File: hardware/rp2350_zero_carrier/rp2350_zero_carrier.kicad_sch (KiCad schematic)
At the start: 8 parts, among them J1 RP2350-Zero_Header(20pin,plac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, J2 USB-A_Host(Neltron_5075AR-04-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, SW1 1回路2接点スイッチ(3pin,NKK_115643,ON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, SW2 1回路2接点スイッチ(3pin,NKK_115643,ON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, SW3 1回路2接点スイッチ(3pin,NKK_115643,ON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

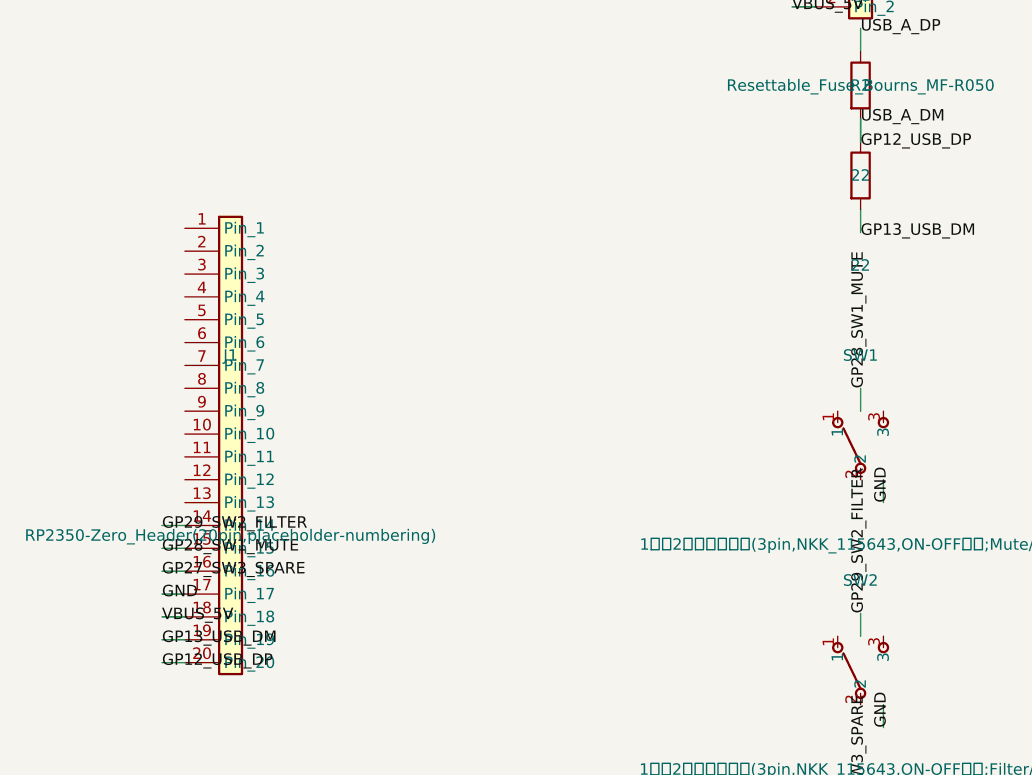
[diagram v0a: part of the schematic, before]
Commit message: feat: unify game mode and add Sumeru lyre mapping
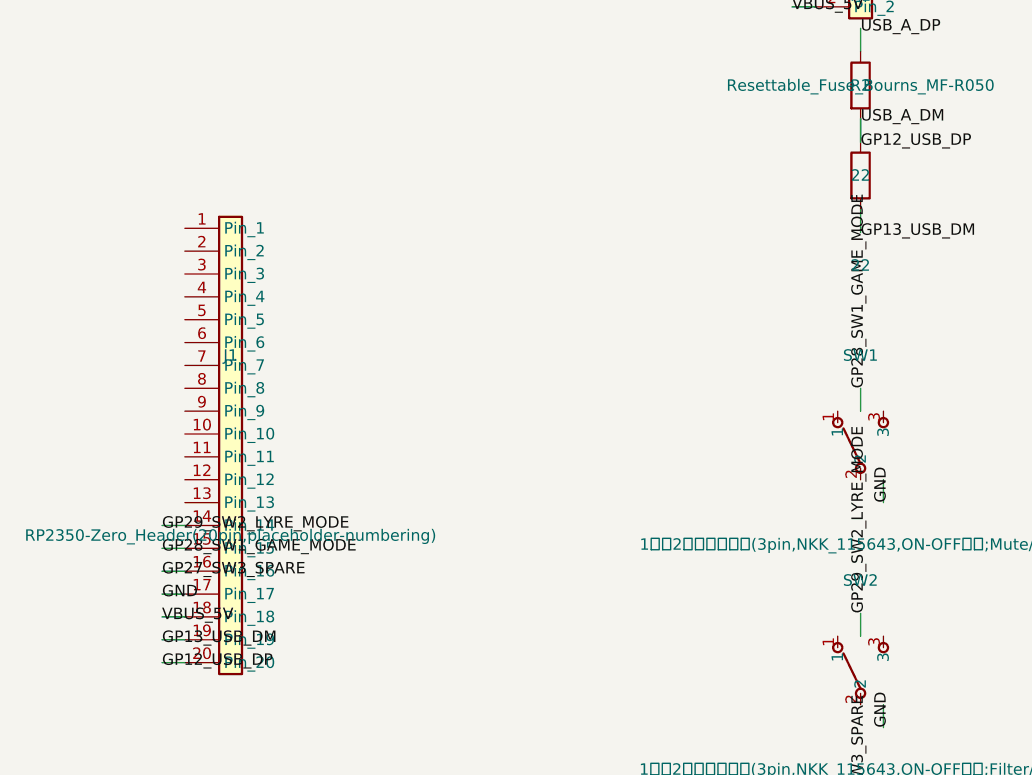
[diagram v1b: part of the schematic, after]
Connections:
- net GP28_SW1_MUTE renamed GP28_SW1_GAME_MODE
- net GP29_SW2_FILTER renamed GP29_SW2_LYRE_MODE
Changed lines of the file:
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@@
   (label "GND" (at 32.38 146.51 0) (effects (font (size 1.27 1.27)) (justify left)))
   (label "GP27_SW3_SPARE" (at 32.38 143.97 0) (effects (font (size 1.27 1.27)) (justify left)))
-  (label "GP28_SW1_MUTE" (at 32.38 141.43 0) (effects (font (size 1.27 1.27)) (justify left)))
-  (label "GP29_SW2_FILTER" (at 32.38 138.89 0) (effects (font (size 1.27 1.27)) (justify left)))
+  (label "GP28_SW1_GAME_MODE" (at 32.38 141.43 0) (effects (font (size 1.27 1.27)) (justify left)))
+  (label "GP29_SW2_LYRE_MODE" (at 32.38 138.89 0) (effects (font (size 1.27 1.27)) (justify left)))
   (label "GP12_USB_DP" (at 110 96.35 0) (effects (font (size 1.27 1.27)) (justify left)))
   (label "USB_A_DP" (at 110 83.65 0) (effects (font (size 1.27 1.27)) (justify left)))
@@
   (label "USB_A_DP" (at 152.38 88.73 0) (effects (font (size 1.27 1.27)) (justify left)))
   (label "GND" (at 152.38 86.19 0) (effects (font (size 1.27 1.27)) (justify left)))
-  (label "GP28_SW1_MUTE" (at 110 123.65 90) (effects (font (size 1.27 1.27)) (justify left)))
+  (label "GP28_SW1_GAME_MODE" (at 110 123.65 90) (effects (font (size 1.27 1.27)) (justify left)))
   (label "GND" (at 112.54 136.35 90) (effects (font (size 1.27 1.27)) (justify left)))
-  (label "GP29_SW2_FILTER" (at 110 148.65 90) (effects (font (size 1.27 1.27)) (justify left)))
+  (label "GP29_SW2_LYRE_MODE" (at 110 148.65 90) (effects (font (size 1.27 1.27)) (justify left)))
   (label "GND" (at 112.54 161.35 90) (effects (font (size 1.27 1.27)) (justify left)))
   (label "GP27_SW3_SPARE" (at 110 173.65 90) (effects (font (size 1.27 1.27)) (justify left)))
